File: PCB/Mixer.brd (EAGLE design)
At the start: 110 x 110 mm, 207 parts, among them U1 TL074IDT, U10 POWER, U11 TL074IDT, U12 3PDTSWITCH, U2 TL074IDT, U3 TL074IDT, U4 TL074IDT, U5 TL074IDT, U6 TL074IDT, U7 TL074IDT, U8 22PINHEADER22PINHEADER, U9 22PINHEADER22PINHEADER

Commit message: Add switch and analog selectors
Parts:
- added R82, R83: 10k, lib:R0603
- moved CH1:C1 111.8 mm to (26.0, 98.8)
- moved CH1:C2 111.2 mm to (26.1, 91.8)
- moved CH3:C2 97.0 mm to (54.0, 91.6)
- moved CH2:C2 96.6 mm to (40.1, 91.6)
- moved CH2:C1 93.2 mm to (40.0, 98.6)
- moved CH3:C1 89.5 mm to (53.9, 98.6)
- moved CH1:U2 86.0 mm to (25.9, 78.9)
- moved CH3:U2 78.1 mm to (53.9, 78.5)
- moved CH2:U2 72.9 mm to (40.9, 78.7)
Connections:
- new net LED_GREEN: R83.2, U12.P$4, U9.22
- new net LED_RED: R82.2, U12.P$6, U9.21
- new net SELECTOR: U12.P$2
- net +9V: now also U12.P$1, U12.P$5
- net GND: now also R82.1, R83.1, U12.P$3

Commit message: Semi done
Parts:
- added C31, C32: 100n/16V, lib:0603
- added C33: 10u / 16V, lib:0603
- added CH1:R17, CH2:R17, CH3:R17: 100R, lib:R0603
- added R84: 1k, lib:R0603
- added U13: ISL43240IAZ, lib:SOP65P777X173-20N
- added U14: ISL43410IUZ, lib:SOP50P490X110-10N
- moved R83 464.1 mm to (86.4, 12.1), turned to 180 degrees
- moved R82 462.0 mm to (86.4, 15.3), turned to 180 degrees
- moved C29 392.1 mm to (87.6, 67.3), turned to 180 degrees
- moved R81 389.3 mm to (83.8, 33.0)
- moved R80 388.7 mm to (83.8, 36.2)
- moved R73 385.7 mm to (80.0, 59.1)
- moved R78 385.1 mm to (84.5, 52.7)
- moved C30 384.8 mm to (72.4, 67.3), turned to 90 degrees
- moved R74 382.3 mm to (80.0, 66.0)
- moved R77 379.0 mm to (74.3, 47.0)
- moved R76 374.9 mm to (80.0, 55.9)
- moved C28 374.0 mm to (87.6, 59.7), turned to 180 degrees
- moved U11 373.0 mm to (71.8, 54.0)
- moved R69 369.9 mm to (80.0, 62.2), turned to 180 degrees
- moved R72 369.5 mm to (80.0, 52.7), turned to 180 degrees
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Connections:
- removed net CH1:N$13: CH1:R10.2, CH1:R5.2, CH1:R8.1, CH1:U2.1
- removed net CH2:N$13: CH2:R10.2, CH2:R5.2, CH2:R8.1, CH2:U2.1
- removed net CH3:N$13: CH3:R10.2, CH3:R5.2, CH3:R8.1, CH3:U2.1
- removed net MONITOR_VOLUME5_P4: U7.12
- removed net V+: U6.4
- removed net V-: U6.11
- new net MASTER_BYP: R20.1, U14.3, U14.7, U2.1, U2.2
- new net MASTER_OUT_L: U14.8, U5.12, U6.3
- new net MASTER_OUT_R: U14.2, U3.3, U5.5
- new net SR_BYP_CH1: CH1:R10.2, CH1:R5.2, CH1:R8.1, CH1:U2.1, U13.4
- new net SR_BYP_CH2: CH2:R10.2, CH2:R5.2, CH2:R8.1, CH2:U2.1, U13.7
- new net SR_BYP_CH3: CH3:R10.2, CH3:R5.2, CH3:R8.1, CH3:U2.1, U13.14
- new net SR_OUT_CH1: CH1:R17.2, U13.2
- new net SR_OUT_CH2: CH2:R17.2, U13.9
- new net SR_OUT_CH3: CH3:R17.2, U13.12
- new net SR_SEL_CH1: CH1:R16.1, U13.3
- new net SR_SEL_CH2: CH2:R16.1, U13.8
- new net SR_SEL_CH3: CH3:R16.1, U13.13
- net +9V: now also C30.2, C31.1, C32.1, C33.2, U13.16, U14.10, U6.4
- net GAIN1_P3_CH1: now also CH1:R17.1; no longer CH1:R16.1
- net GAIN1_P3_CH2: now also CH2:R17.1; no longer CH2:R16.1
- net GAIN1_P3_CH3: now also CH3:R17.1; no longer CH3:R16.1
- net GND: now also C30.1, C31.2, C32.2, C33.1, U12.P$7, U12.P$8, U12.P$9, U13.5, U13.6, U14.4, U14.5, U6.11
- net MASTER_RETURN_L: now also U14.9; no longer U5.12, U6.3
- net MASTER_RETURN_R: now also U14.1; no longer U3.3, U5.5
- net MONITOR_VOLUME5_P5: now also U7.12
- net N$15: now also R84.1, U12.P$2; no longer R20.1, U2.1, U2.2
- net SELECTOR: now also R84.2, U13.1, U13.10, U13.11, U13.20, U14.6; no longer U12.P$2
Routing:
- net +9V: track 0.00 -> 424.5 mm, vias 0 -> 19
- net VDD: track 0.00 -> 344.1 mm, vias 0 -> 17
- net MASTER_RETURN_R: track 0.00 -> 155.8 mm, vias 0 -> 3
- net N$30: track 0.00 -> 151.0 mm, vias 0 -> 4
- net VEE: track 0.00 -> 149.1 mm, vias 0 -> 9
- net MASTER_VOLUME2_P2: track 0.00 -> 127.7 mm, vias 0 -> 3
- net MASTER_VOLUME2_P3: track 0.00 -> 126.2 mm, vias 0 -> 2
- net VOL1_P3_CH3: track 0.00 -> 124.7 mm, vias 0 -> 1
- net LED_RED: track 0.00 -> 114.1 mm
- net MONITOR_VOLUME3_P3: track 0.00 -> 113.3 mm, vias 0 -> 1
- net GAIN1_P2_CH3: track 0.00 -> 112.8 mm, vias 0 -> 1
- net MONITOR_VOLUME4_P6: track 0.00 -> 111.4 mm, vias 0 -> 1
- net MONITOR_VOLUME4_P3: track 0.00 -> 110.1 mm, vias 0 -> 1
- net MONITOR_VOLUME3_P6: track 0.00 -> 107.4 mm, vias 0 -> 1
- net MONITOR_VOLUME5_P6: track 0.00 -> 103.7 mm, vias 0 -> 1
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- added copper zone on layer 1, net GND
- added copper zone on layer 15, net GND
- added copper zone on layer 16, net GND
- added copper zone on layer 2, net GND

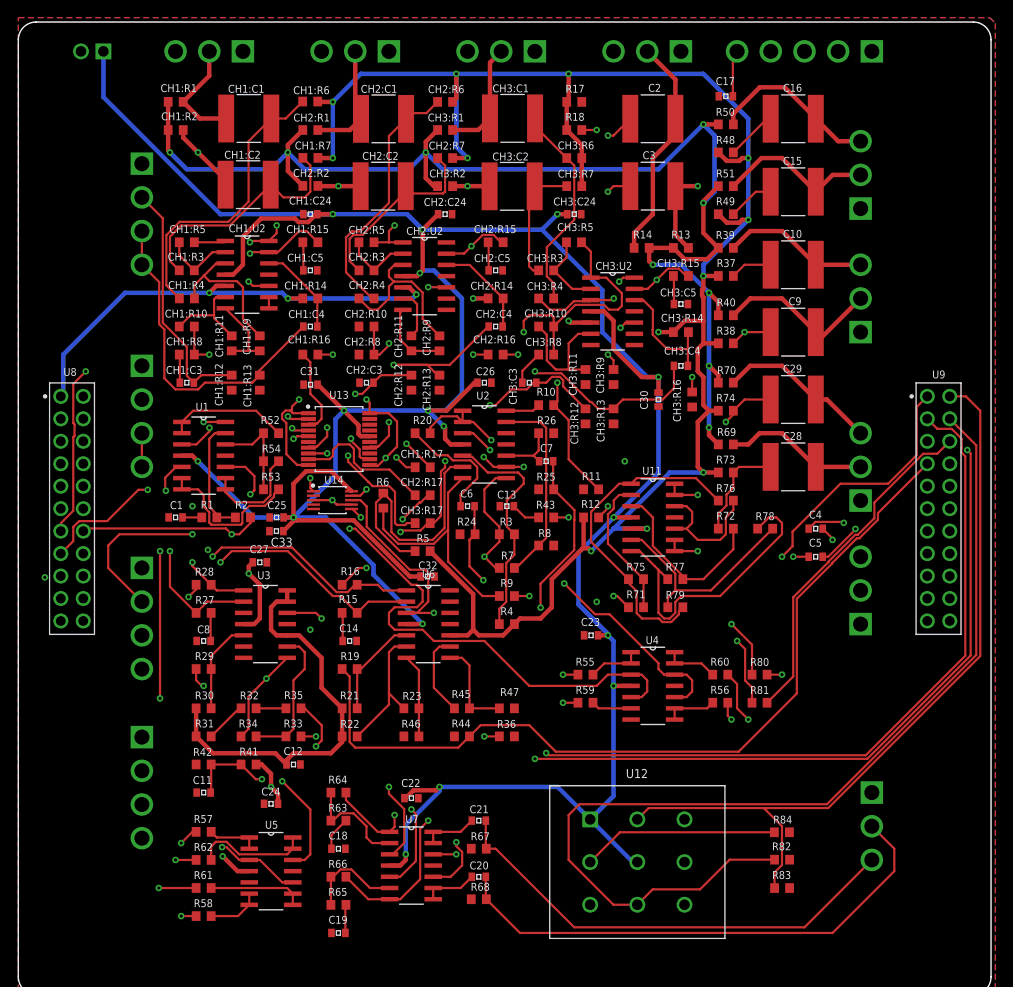
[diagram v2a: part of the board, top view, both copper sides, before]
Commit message: Fixed wiring on main board
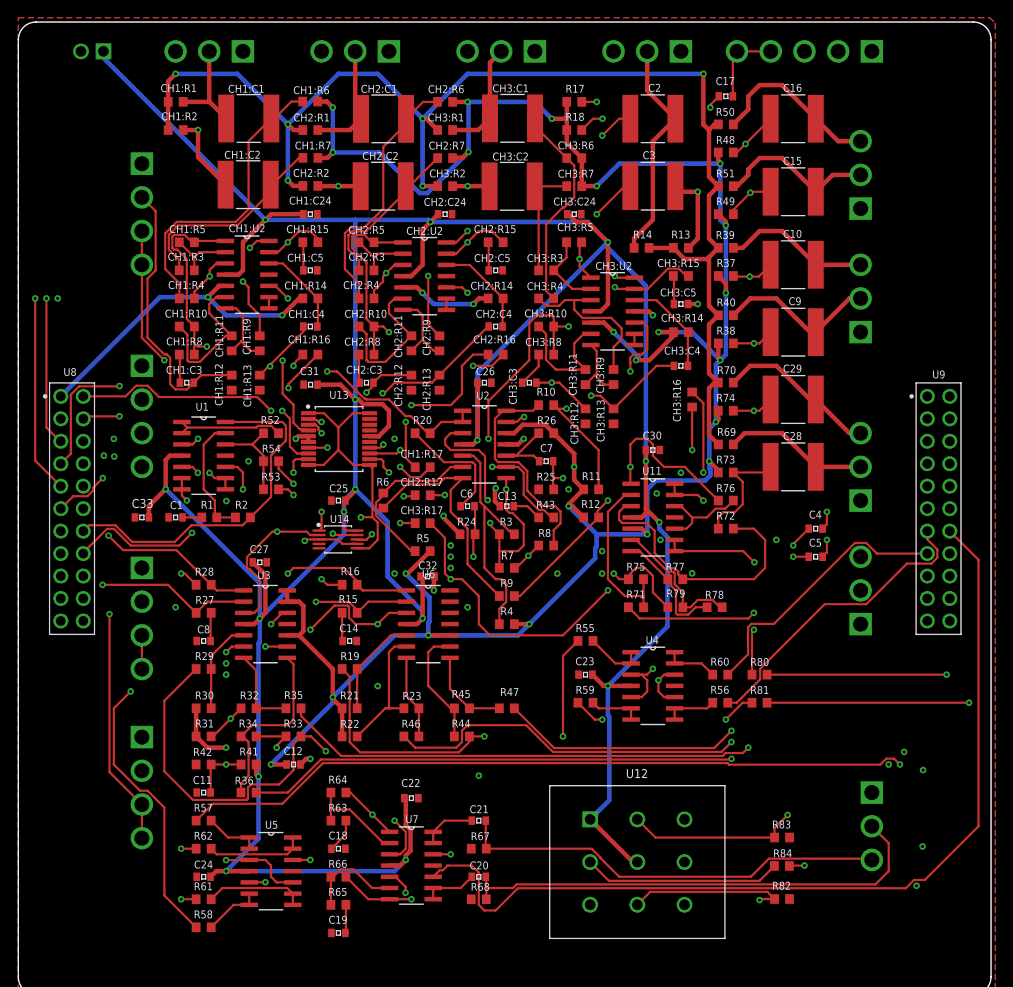
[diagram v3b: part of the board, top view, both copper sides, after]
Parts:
- moved R36 29.9 mm to (26.0, 22.9)
- moved C33 15.3 mm to (14.0, 54.0)
- moved C24 11.2 mm to (21.0, 13.3)
- moved R78 10.6 mm to (78.7, 43.8)
- moved C25 7.24 mm to (36.2, 55.9)
- moved C30 5.75 mm to (71.8, 61.6), turned to 180 degrees
- moved R83 5.71 mm to (86.4, 17.8)
- moved U14 4.49 mm to (36.2, 51.5)
- moved C23 4.49 mm to (64.1, 36.2)
- moved R82 4.45 mm to (86.4, 10.8)
- moved R55 3.81 mm to (64.1, 40.0)
- moved R84 3.81 mm to (86.4, 14.6)
- moved R62 1.27 mm to (21.0, 16.5)
- moved R58 1.27 mm to (21.0, 7.62)
- moved R57 1.27 mm to (21.0, 19.7)
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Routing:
- net N$29: track 4.75 -> 115.5 mm, vias 0 -> 2
- net N$52: track 5.92 -> 109.7 mm, vias 0 -> 2
- net N$51: track 5.80 -> 100.0 mm, vias 0 -> 2
- net SELECTOR: track 34.0 -> 126.6 mm, vias 4 -> 3
- net MASTER_OUT_R: track 0.00 -> 61.7 mm, vias 0 -> 2
- net MASTER_RETURN_L: track 60.7 -> 115.4 mm, vias 2 -> 4
- net PRE_TC: track 87.1 -> 137.5 mm, vias 3 -> 4
- net N$30: track 151.0 -> 104.7 mm, vias 4 -> 2
- net SR_SEL_CH3: track 0.00 -> 41.5 mm, vias 0 -> 2
- net GAIN1_P3_CH2: track 47.7 -> 87.8 mm, vias 1 -> 3
- net MASTER_RETURN_R: track 155.8 -> 116.3 mm, vias 3 -> 4
- net GAIN1_P3_CH3: track 81.5 -> 115.1 mm
- net GAIN1_P2: track 96.1 -> 65.0 mm, vias 3 -> 1
- net VDD: track 344.1 -> 373.9 mm, vias 17 -> 28
- net MONITOR_VOLUME1_P6: track 54.0 -> 83.1 mm, vias 1 -> 2
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
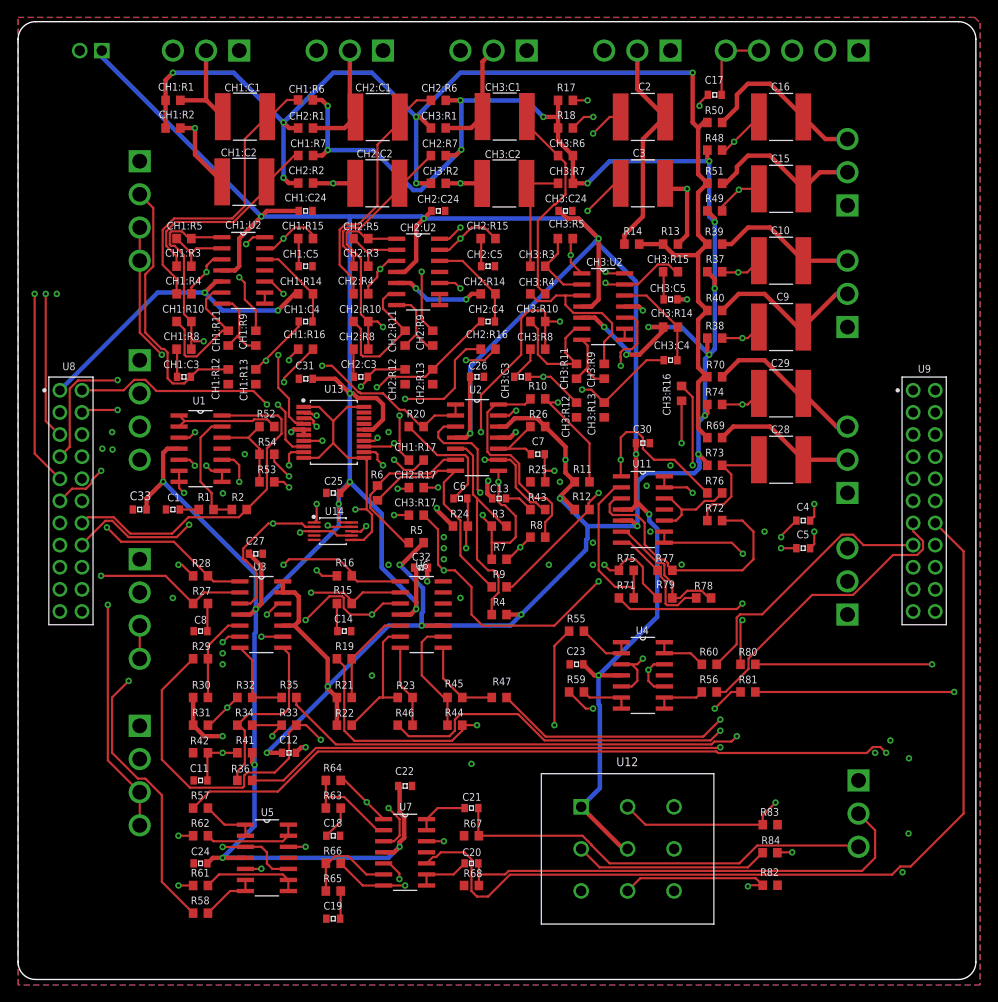
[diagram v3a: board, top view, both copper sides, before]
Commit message: Updating to 2 layer
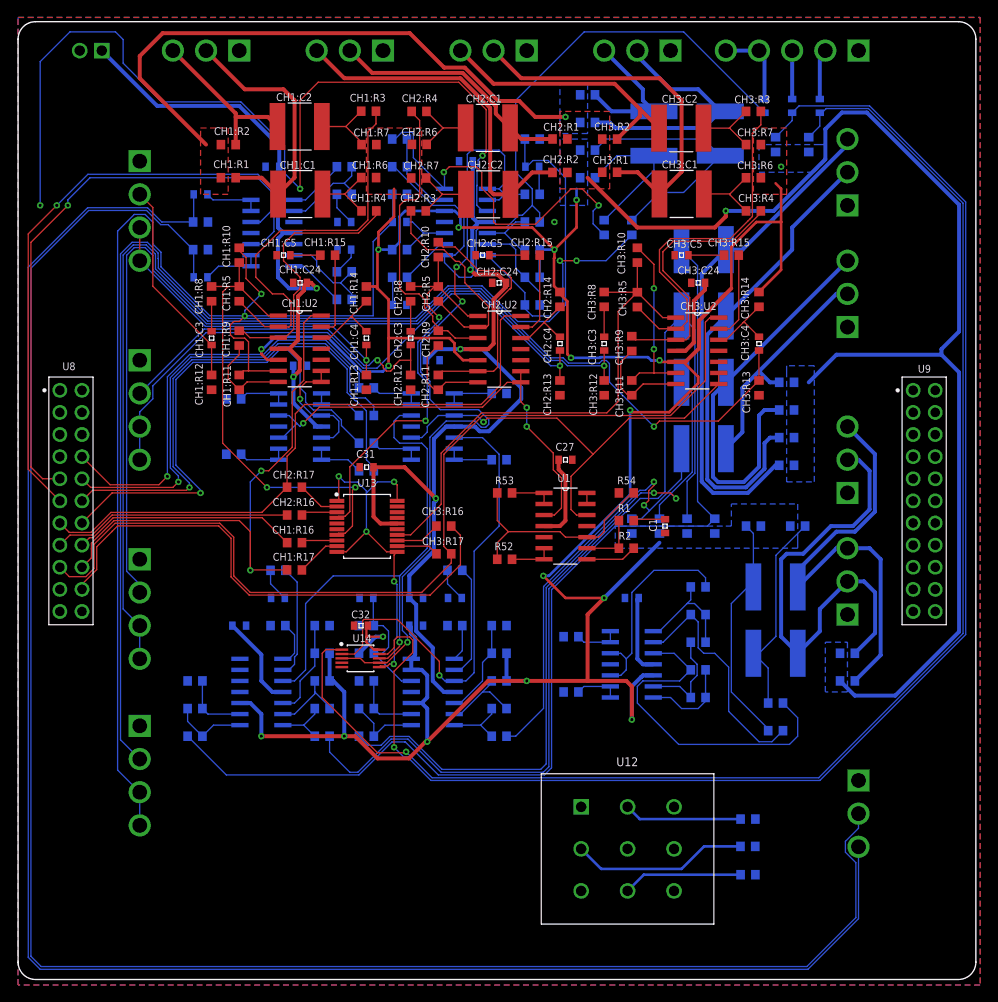
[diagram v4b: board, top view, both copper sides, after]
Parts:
- moved R68 79.4 mm to (21.0, 83.8), flipped to the bottom
- moved C21 77.0 mm to (21.0, 90.2), flipped to the bottom
- moved R67 77.0 mm to (21.0, 87.0), flipped to the bottom
- moved C19 76.8 mm to (37.5, 83.8), flipped to the bottom, turned to 0 degrees
- moved C20 74.2 mm to (21.0, 80.6), flipped to the bottom
- moved C22 72.7 mm to (29.2, 93.3), flipped to the bottom
- moved U7 72.7 mm to (29.2, 85.7), flipped to the bottom
- moved R65 71.1 mm to (37.5, 81.3), flipped to the bottom
- moved C18 70.5 mm to (37.5, 87.0), flipped to the bottom
- moved R63 70.5 mm to (37.5, 90.2), flipped to the bottom
- moved R64 70.5 mm to (37.5, 93.3), flipped to the bottom
- moved R66 64.8 mm to (37.5, 78.1), flipped to the bottom
- moved C24 63.6 mm to (47.6, 71.1), flipped to the bottom
- moved R60 62.5 mm to (24.8, 66.7), flipped to the bottom
- moved R58 62.3 mm to (55.2, 59.7), flipped to the bottom
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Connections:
- removed net CH1:N$9: CH1:U2.8, CH1:U2.9
- removed net CH2:N$9: CH2:U2.8, CH2:U2.9
- removed net CH3:N$9: CH3:U2.8, CH3:U2.9
- net CH1_OUT: now also CH1:U2.8, CH1:U2.9, U1.5; no longer U1.3
- net CH2_OUT: now also CH2:U2.8, CH2:U2.9, U1.3; no longer U1.5
- net CH3_OUT: now also CH3:U2.8, CH3:U2.9, U1.12; no longer U1.10
- net GAIN1_P2: now also U9.6; no longer U8.17
- net GAIN1_P2_CH1: now also U9.18; no longer U8.5
- net GAIN1_P2_CH2: now also U9.16; no longer U8.9
- net GAIN1_P2_CH3: now also U8.12; no longer U8.13
- net GAIN1_P3_CH1: now also U8.14; no longer U8.6
- net GAIN1_P3_CH2: now also U8.7; no longer U8.10
- net GAIN1_P3_CH3: now also U8.9; no longer U8.14
- net GAIN2_P2: now also U9.5; no longer U8.19
- net MASTER_VOLUME1_P2: now also U8.4; no longer U8.15
- net MASTER_VOLUME1_P3: now also U1.8, U9.10; no longer U1.14, U8.16
- net MONITOR_VOLUME1_P3: now also U8.17; no longer U9.6
- net MONITOR_VOLUME1_P6: now also U8.18; no longer U9.5
- net MONITOR_VOLUME3_P3: now also U8.16; no longer U9.10
- net MONITOR_VOLUME4_P3: now also U8.19; no longer U9.12
- net MONITOR_VOLUME5_P2: now also U8.6; no longer U9.16
- net MONITOR_VOLUME5_P5: now also U8.5; no longer U9.18
- net N$1: now also U1.10; no longer U1.12
- net N$2: now also U1.9; no longer U1.13
- net N$33: now also U1.6, U1.7; no longer U1.1, U1.2
- net N$36: now also U1.1, U1.2; no longer U1.6, U1.7
- net N$39: now also U1.13, U1.14; no longer U1.8, U1.9
- net PRE_TC: now also U9.12; no longer U8.18
- net SR_BYP_CH1: now also U13.7; no longer U13.4
- net SR_BYP_CH2: now also U13.4; no longer U13.7
- net SR_OUT_CH1: now also U13.9; no longer U13.2
- net SR_OUT_CH2: now also U13.2; no longer U13.9
- net SR_SEL_CH1: now also U13.8; no longer U13.3
- net SR_SEL_CH2: now also U13.3; no longer U13.8
- net VOL1_P2_CH2: now also U8.10; no longer U8.7
- net VOL1_P3_CH1: now also U8.15; no longer U8.4
- net VOL1_P3_CH3: now also U8.13; no longer U8.12
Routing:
- net +9V: track 427.7 -> 227.6 mm, vias 16 -> 6
- net N$62: track 49.1 -> 211.5 mm
- net N$61: track 54.7 -> 216.1 mm
- net MASTER_VOLUME2_P2: track 144.1 -> 0.00 mm, vias 2 -> 0
- net MONITOR_VOLUME4_P6: track 125.8 -> 0.00 mm, vias 1 -> 0
- net VOL1_P2_CH3: track 113.5 -> 0.00 mm, vias 2 -> 0
- net MONITOR_VOLUME5_P6: track 114.0 -> 6.65 mm, vias 2 -> 0
- net MONITOR_VOLUME3_P6: track 105.6 -> 0.00 mm, vias 1 -> 0
- net MASTER_VOLUME2_P3: track 104.9 -> 0.00 mm, vias 1 -> 0
- net GAIN1_P2_CH3: track 115.0 -> 10.1 mm, vias 2 -> 0
- net MONITOR_VOLUME5_P3: track 108.7 -> 6.52 mm, vias 1 -> 0
- net MASTER_VOLUME2_P5: track 101.5 -> 0.00 mm, vias 2 -> 0
- net MONITOR_MIX_L: track 100.0 -> 0.00 mm, vias 1 -> 0
- net MONITOR_MIX_R: track 92.1 -> 0.00 mm, vias 2 -> 0
- net LED_GREEN: track 101.7 -> 13.6 mm, vias 1 -> 0
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- added copper zone on layer 1, net VDD
- added copper zone on layer 16, net VDD
- added copper zone on layer 1, net VEE
- added copper zone on layer 16, net VEE
